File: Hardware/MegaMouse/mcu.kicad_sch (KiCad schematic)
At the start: 19 parts, among them J401 ICSP, SW401 RESET, SW402 START/MODE, U401 ATmega328P, Y401 16mHz

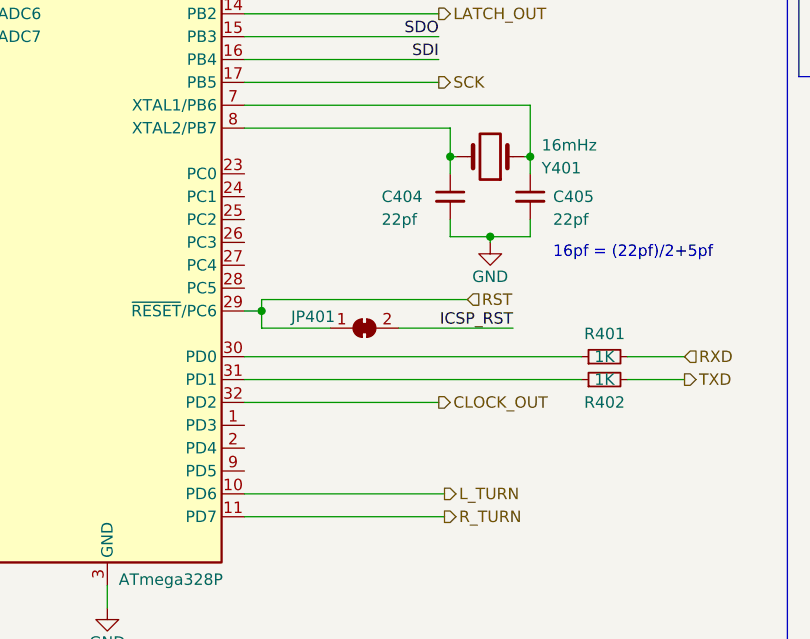
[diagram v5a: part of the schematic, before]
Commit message: Add inital photodiodes
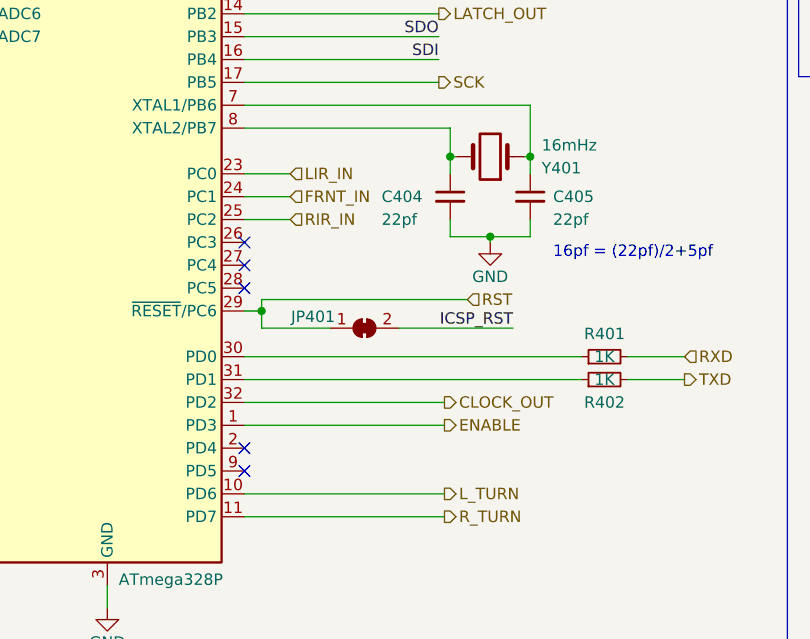
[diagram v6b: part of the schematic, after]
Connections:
- net ENABLE: now reaches U401.1 (PD3)
- net LIR_IN: now reaches U401.23 (PC0)
- net FRNT_IN: now reaches U401.24 (PC1)
- net RIR_IN: now reaches U401.25 (PC2)
- no-connect marks 6 -> 11
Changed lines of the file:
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@@
   (junction (at 59.69 86.995) (diameter 0) (color 0 0 0 0)
   )
+  (no_connect (at 57.785 102.235))
   (no_connect (at 27.305 56.515))
   (no_connect (at 48.26 154.94))
   (no_connect (at 48.26 157.48))
   (no_connect (at 48.26 152.4))
+  (no_connect (at 57.785 79.375))
   (no_connect (at 35.56 152.4))
+  (no_connect (at 57.785 104.775))
+  (no_connect (at 57.785 81.915))
   (no_connect (at 27.305 53.975))
+  (no_connect (at 57.785 84.455))
+  (wire (pts (xy 62.865 76.835) (xy 57.785 76.835))
+    (stroke (width 0) (type default) (color 0 0 0 0))
+  )
   (wire (pts (xy 57.785 53.975) (xy 79.375 53.975))
     (stroke (width 0) (type default) (color 0 0 0 0))
@@
     (stroke (width 0) (type default) (color 0 0 0 0))
   )
-  (wire (pts (xy 79.375 97.155) (xy 57.785 97.155))
+  (wire (pts (xy 80.01 97.155) (xy 57.785 97.155))
     (stroke (width 0) (type default) (color 0 0 0 0))
   )
@@
     (stroke (width 0) (type default) (color 0 0 0 0))
   )
+  (wire (pts (xy 80.01 99.695) (xy 57.785 99.695))
+    (stroke (width 0) (type default) (color 0 0 0 0))
+  )
   (wire (pts (xy 48.26 149.86) (xy 50.165 149.86))
     (stroke (width 0) (type default) (color 0 0 0 0))
@@
     (stroke (width 0) (type default) (color 0 0 0 0))
   )
+  (wire (pts (xy 62.865 71.755) (xy 57.785 71.755))
+    (stroke (width 0) (type default) (color 0 0 0 0))
+  )
   (wire (pts (xy 38.1 35.56) (xy 38.1 36.83))
     (stroke (width 0) (type default) (color 0 0 0 0))
@@
   )
   (wire (pts (xy 69.85 159.385) (xy 74.93 159.385))
+    (stroke (width 0) (type default) (color 0 0 0 0))
+  )
+  (wire (pts (xy 62.865 74.295) (xy 57.785 74.295))
     (stroke (width 0) (type default) (color 0 0 0 0))
   )
@@
     (effects (font (size 1.27 1.27)) (justify left bottom))
   )
+  (hierarchical_label "FRNT_IN" (shape input) (at 62.865 74.295 0)
+    (effects (font (size 1.27 1.27)) (justify left))
+  )
   (hierarchical_label "RST" (shape input) (at 82.55 85.725 0)
     (effects (font (size 1.27 1.27)) (justify left))
@@
     (effects (font (size 1.27 1.27)) (justify right))
   )
-  (hierarchical_label "CLOCK_OUT" (shape output) (at 79.375 97.155 0)
+  (hierarchical_label "CLOCK_OUT" (shape output) (at 80.01 97.155 0)
     (effects (font (size 1.27 1.27)) (justify left))
   )
@@
     (effects (font (size 1.27 1.27)) (justify left))
   )
+  (hierarchical_label "LIR_IN" (shape input) (at 62.865 71.755 0)
+    (effects (font (size 1.27 1.27)) (justify left))
+  )
   (hierarchical_label "L_TURN" (shape output) (at 80.01 107.315 0)
     (effects (font (size 1.27 1.27)) (justify left))
   )
+  (hierarchical_label "ENABLE" (shape output) (at 80.01 99.695 0)
+    (effects (font (size 1.27 1.27)) (justify left))
+  )
   (hierarchical_label "LATCH_OUT" (shape output) (at 79.375 53.975 0)
     (effects (font (size 1.27 1.27)) (justify left))
@@
     (effects (font (size 1.27 1.27)) (justify left))
   )
+  (hierarchical_label "RIR_IN" (shape input) (at 62.865 76.835 0)
+    (effects (font (size 1.27 1.27)) (justify left))
+  )

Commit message: Add in some more, random junk
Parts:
- removed C403: 100nF, Capacitor_SMD:C_0805_2012Metric, symbol Device:C_Small
- added C405: 100nF, Capacitor_SMD:C_0805_2012Metric, symbol Device:C_Small
- added TP406: TestPoint, TestPoint:TestPoint_Pad_2.0x2.0mm, symbol Connector:TestPoint
- added U402: SN74HC595, KenwoodFox:SN74HC595, symbol KenwoodFox:SN74HC595
- renumbered C404 to C403, C405 to C404
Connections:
- net +5V: now also C405.1, U402.10 (SRCLR), U402.16 (VCC)
- net CLOCK_OUT: now also U401.2 (PD4), U402.11 (SRCLK); no longer U401.32 (PD2)
- net DATA_OUT: now also U402.9 (QH'); no longer U401.13 (PB1)
- net ENABLE: now also U402.15 (QA); no longer U401.1 (PD3)
- net GND: now also C405.2, U402.13 (OE), U402.8 (GND)
- net LATCH_OUT: now also U402.12 (RCLK)
- net L_TURN: now also U402.1 (QB); no longer U401.10 (PD6)
- net R_TURN: now also U402.2 (QC); no longer U401.11 (PD7)
- net L_ENC_B: now reaches U401.26 (PC3)
- net R_ENC_B: now reaches U401.27 (PC4)
- net R_MOT_1: now reaches U401.28 (PC5)
- net R_MOT_2: now reaches U401.9 (PD5)
- new net: TP406.1, U402.7 (QH)
- new net BRAKE: U402.3 (QD)
- new net DATA: U401.13 (PB1), U402.14 (SER)
- new net L_ENC_A: U401.32 (PD2)
- new net L_MOT_1: U401.10 (PD6)
- new net L_MOT_2: U401.11 (PD7)
- new net R_ENC_A: U401.1 (PD3)
- no-connect marks 11 -> 9
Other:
- moved on the sheet: C402

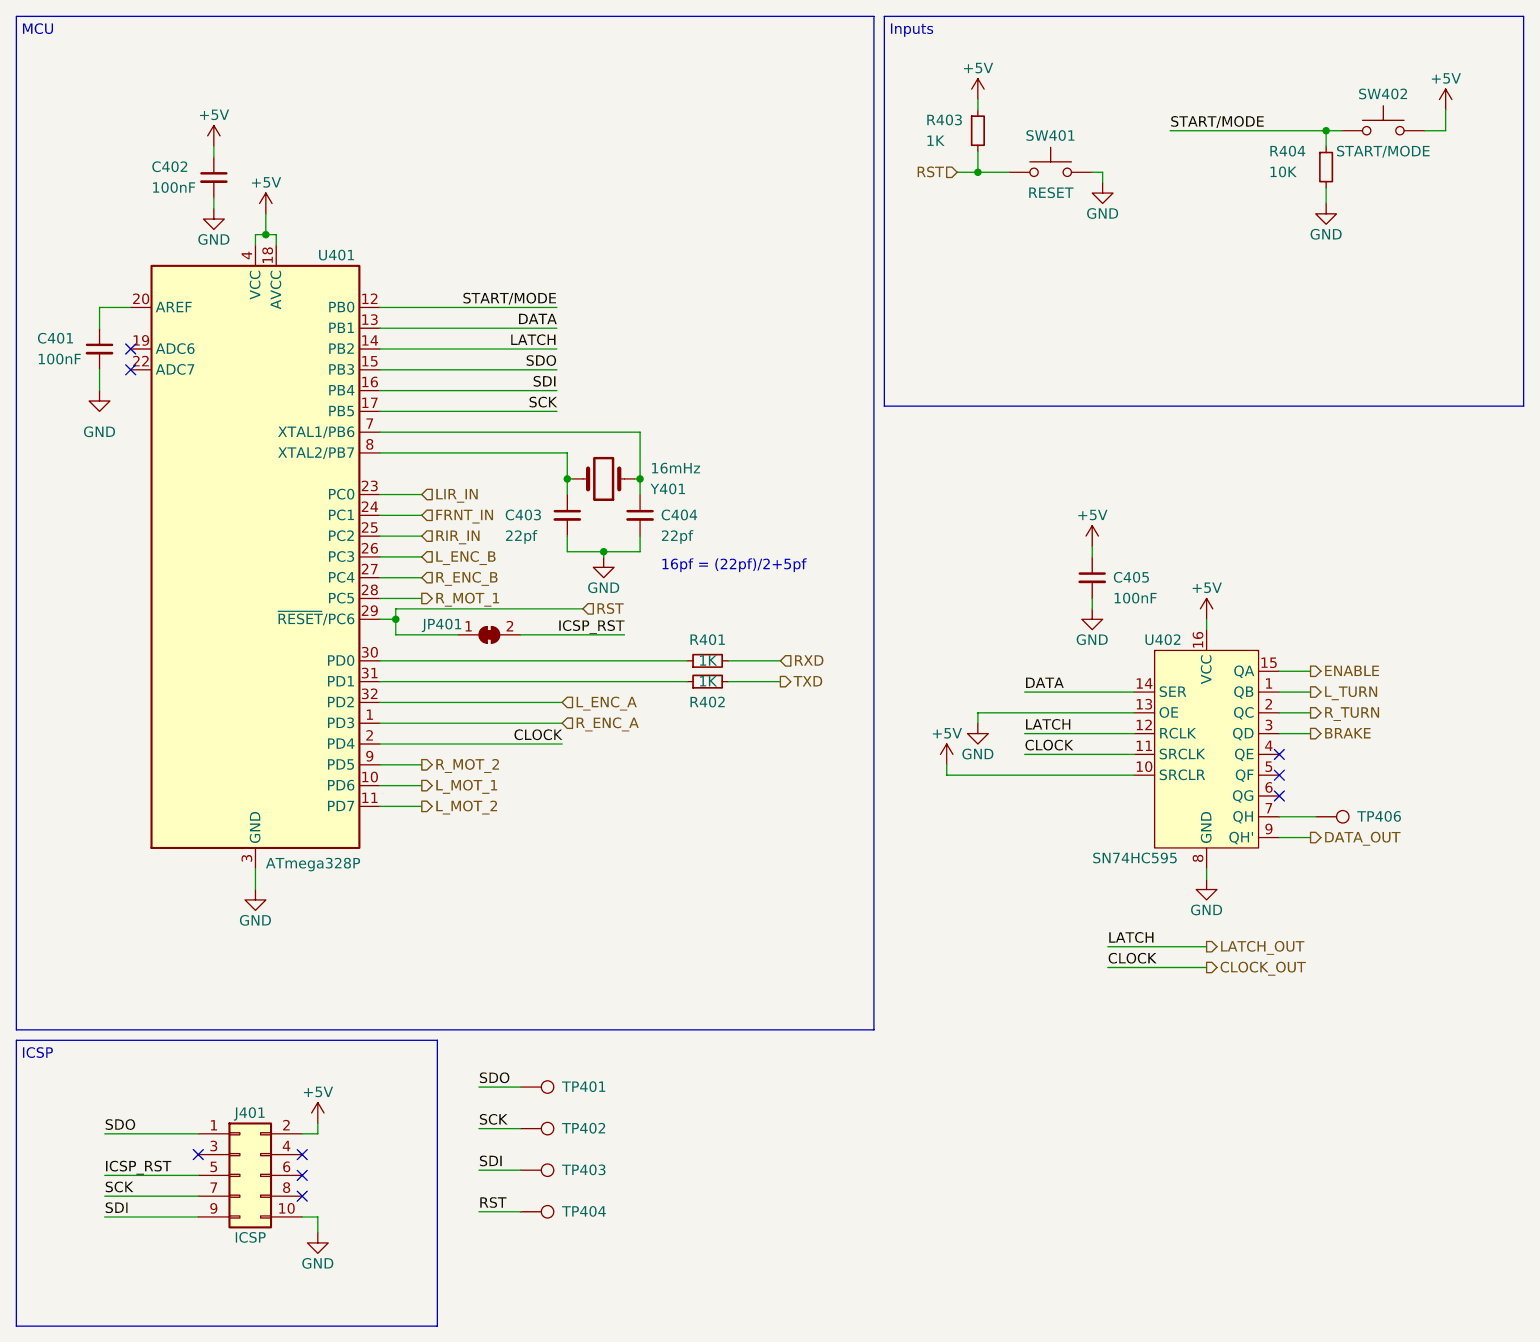
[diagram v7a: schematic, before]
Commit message: Add lines for enabling emittersg
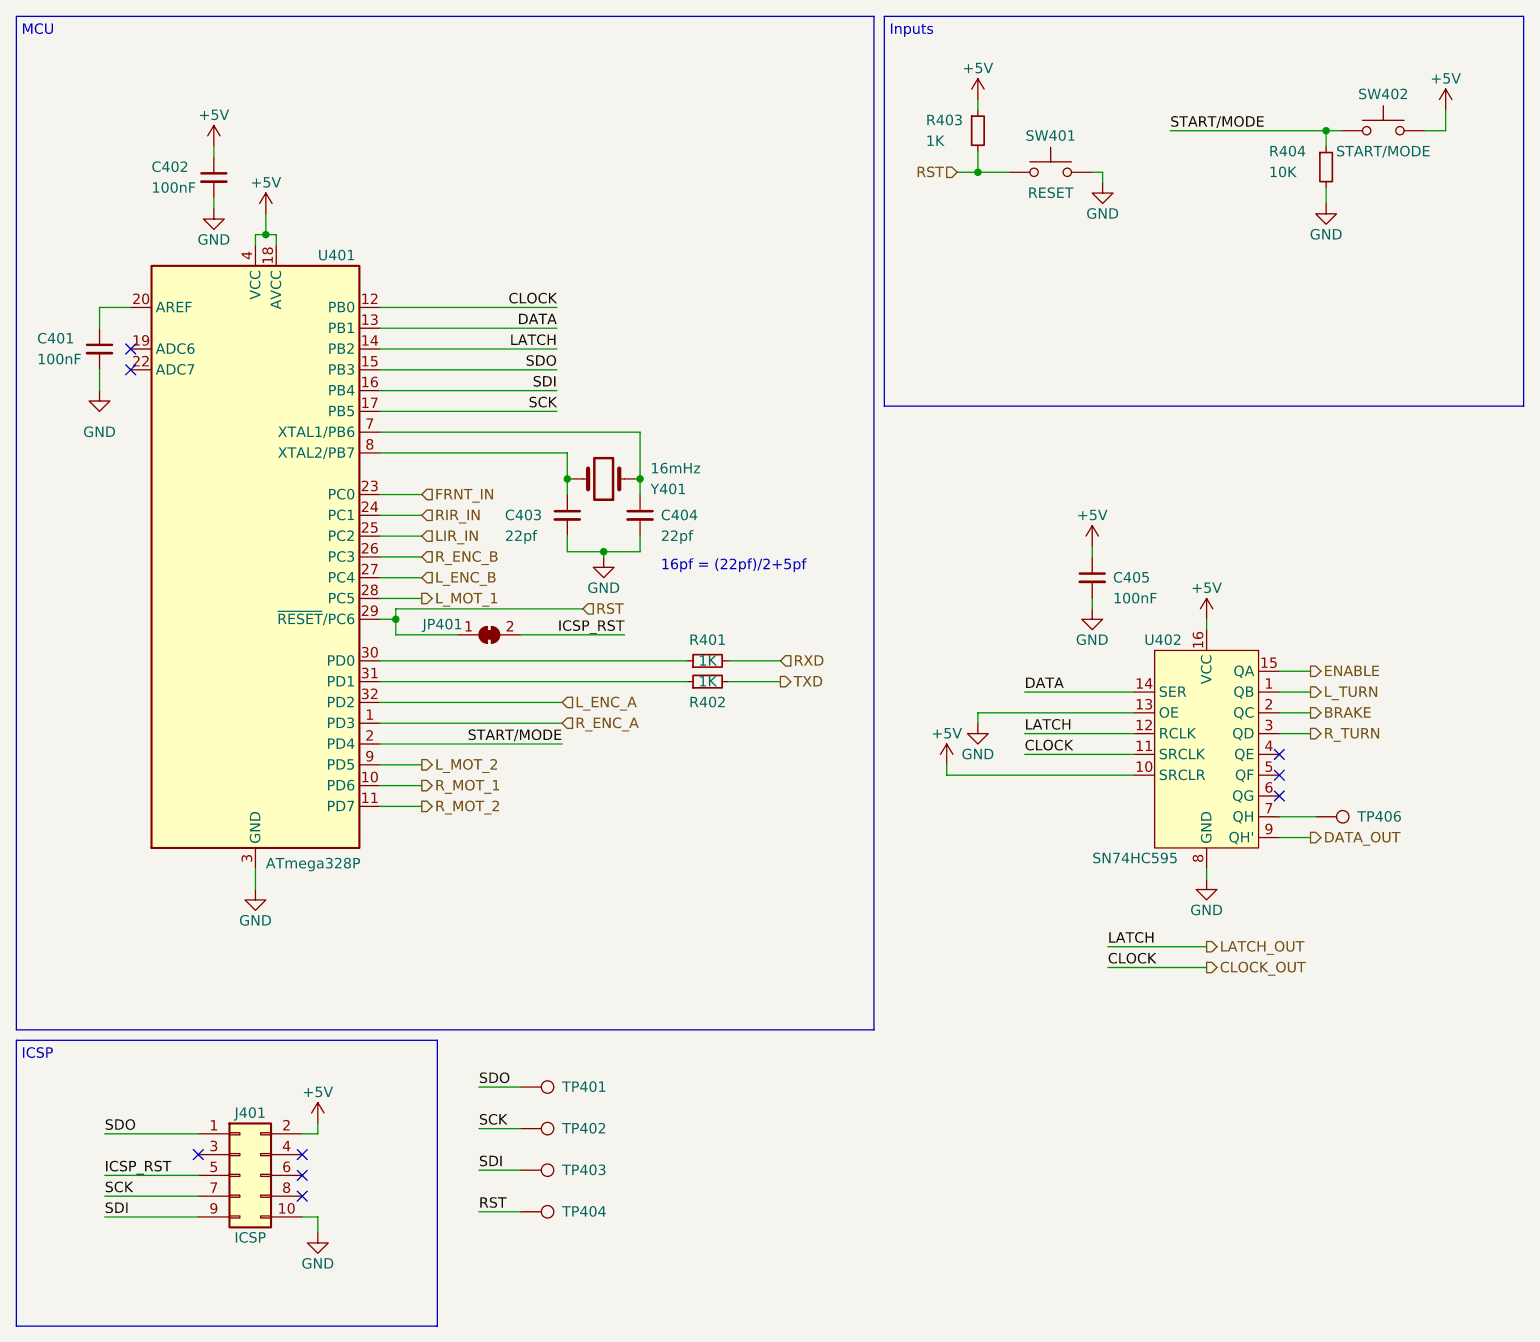
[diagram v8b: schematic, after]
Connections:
- net BRAKE: now also U402.2 (QC); no longer U402.3 (QD)
- net CLOCK_OUT: now also U401.12 (PB0); no longer U401.2 (PD4)
- net FRNT_IN: now also U401.23 (PC0); no longer U401.24 (PC1)
- net LIR_IN: now also U401.25 (PC2); no longer U401.23 (PC0)
- net L_ENC_B: now also U401.27 (PC4); no longer U401.26 (PC3)
- net L_MOT_1: now also U401.28 (PC5); no longer U401.10 (PD6)
- net L_MOT_2: now also U401.9 (PD5); no longer U401.11 (PD7)
- net RIR_IN: now also U401.24 (PC1); no longer U401.25 (PC2)
- net R_ENC_B: now also U401.26 (PC3); no longer U401.27 (PC4)
- net R_MOT_1: now also U401.10 (PD6); no longer U401.28 (PC5)
- net R_MOT_2: now also U401.11 (PD7); no longer U401.9 (PD5)
- net R_TURN: now also U402.3 (QD); no longer U402.2 (QC)
- net START/MODE: now also U401.2 (PD4); no longer U401.12 (PB0)
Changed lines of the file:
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@@
-    (effects (font (size 1.27 1.27)) (justify right bottom))
-  )
-  (label "START{slash}MODE" (at 79.375 48.895 180)
     (effects (font (size 1.27 1.27)) (justify right bottom))
   )
@@
     (effects (font (size 1.27 1.27)) (justify left bottom))
   )
+  (label "CLOCK" (at 79.375 48.895 180)
+    (effects (font (size 1.27 1.27)) (justify right bottom))
+  )
   (label "SDI" (at 69.85 154.305 0)
     (effects (font (size 1.27 1.27)) (justify left bottom))
@@
     (effects (font (size 1.27 1.27)) (justify left bottom))
   )
-  (label "CLOCK" (at 80.01 102.235 180)
+  (label "START{slash}MODE" (at 80.01 102.235 180)
     (effects (font (size 1.27 1.27)) (justify right bottom))
   )
@@
   (label "CLOCK" (at 146.685 129.54 0)
     (effects (font (size 1.27 1.27)) (justify left bottom))
-  )
-  (hierarchical_label "FRNT_IN" (shape input) (at 62.865 74.295 0)
-    (effects (font (size 1.27 1.27)) (justify left))
   )
   (hierarchical_label "RST" (shape input) (at 82.55 85.725 0)
@@
     (effects (font (size 1.27 1.27)) (justify right))
   )
+  (hierarchical_label "LIR_IN" (shape input) (at 62.865 76.835 0)
+    (effects (font (size 1.27 1.27)) (justify left))
+  )
   (hierarchical_label "DATA_OUT" (shape output) (at 171.45 113.665 0)
     (effects (font (size 1.27 1.27)) (justify left))
@@
     (effects (font (size 1.27 1.27)) (justify left))
   )
-  (hierarchical_label "R_ENC_B" (shape input) (at 62.865 81.915 0)
+  (hierarchical_label "L_ENC_B" (shape input) (at 62.865 81.915 0)
     (effects (font (size 1.27 1.27)) (justify left))
   )
@@
     (effects (font (size 1.27 1.27)) (justify left))
   )
-  (hierarchical_label "LIR_IN" (shape input) (at 62.865 71.755 0)
-    (effects (font (size 1.27 1.27)) (justify left))
-  )
-  (hierarchical_label "L_ENC_B" (shape input) (at 62.865 79.375 0)
+  (hierarchical_label "R_ENC_B" (shape input) (at 62.865 79.375 0)
     (effects (font (size 1.27 1.27)) (justify left))
   )
@@
     (effects (font (size 1.27 1.27)) (justify left))
   )
-  (hierarchical_label "L_MOT_1" (shape output) (at 62.865 107.315 0)
+  (hierarchical_label "R_MOT_1" (shape output) (at 62.865 107.315 0)
     (effects (font (size 1.27 1.27)) (justify left))
   )
-  (hierarchical_label "R_MOT_1" (shape output) (at 62.865 84.455 0)
+  (hierarchical_label "L_MOT_1" (shape output) (at 62.865 84.455 0)
     (effects (font (size 1.27 1.27)) (justify left))
   )
-  (hierarchical_label "R_TURN" (shape output) (at 171.45 98.425 0)
+  (hierarchical_label "BRAKE" (shape output) (at 171.45 98.425 0)
+    (effects (font (size 1.27 1.27)) (justify left))
+  )
+  (hierarchical_label "R_TURN" (shape output) (at 171.45 100.965 0)
     (effects (font (size 1.27 1.27)) (justify left))
   )
@@
     (effects (font (size 1.27 1.27)) (justify left))
   )
-  (hierarchical_label "RIR_IN" (shape input) (at 62.865 76.835 0)
+  (hierarchical_label "FRNT_IN" (shape input) (at 62.865 71.755 0)
     (effects (font (size 1.27 1.27)) (justify left))
   )
-  (hierarchical_label "L_MOT_2" (shape output) (at 62.865 109.855 0)
+  (hierarchical_label "RIR_IN" (shape input) (at 62.865 74.295 0)
+    (effects (font (size 1.27 1.27)) (justify left))
+  )
+  (hierarchical_label "R_MOT_2" (shape output) (at 62.865 109.855 0)
     (effects (font (size 1.27 1.27)) (justify left))
   )
@@
     (effects (font (size 1.27 1.27)) (justify left))
   )
-  (hierarchical_label "R_MOT_2" (shape output) (at 62.865 104.775 0)
+  (hierarchical_label "L_MOT_2" (shape output) (at 62.865 104.775 0)
     (effects (font (size 1.27 1.27)) (justify left))
   )
-  (hierarchical_label "BRAKE" (shape output) (at 171.45 100.965 0)
-    (effects (font (size 1.27 1.27)) (justify left))
-  )
